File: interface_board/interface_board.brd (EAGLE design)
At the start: 72 x 56 mm, 103 parts, among them IC1 V7805-1000, IC6 LAN9512-JZX, K1 61400416021, Q6 CTS_32X25_SMD, U1 SFW15R-1STE1LF, U2 SFW15R-1STE1LF, U3 DMG1012T, U5 PAM2306DYPAA

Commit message: picam360
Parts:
- removed C11: UUD1A220MCL1GS(22u), resistor:153CLV-0405
- removed C15: UUD1E100MCL1GS(10u), resistor:153CLV-0405
- moved IC1 6.22 mm to (34.0, 28.8)
- moved R11 0.92 mm to (39.5, 28.4)
- moved R12 0.92 mm to (41.0, 28.4)
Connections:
- removed net 3V3A1: C32.2, C33.2, C34.2, C35.2, C36.2, C37.2, C38.2, FB2.1, IC6.10, IC6.49, IC6.5, IC6.51, IC6.54, IC6.57, IC6.64
- removed net N$47: IC6.1, JP5.D-
- removed net N$48: IC6.2, JP5.D+
- removed net USBD3_N: IC6.3, K1.2
- removed net USBD3_P: IC6.4, K1.3
- new net USB3_N: IC6.3, JP5.D-
- new net USB3_P: IC6.4, JP5.D+
- new net USBD2_N: IC6.1, K1.2
- new net USBD2_P: IC6.2, K1.3
- net +5V: no longer C11.+
- net 3V3A: now also C32.2, C33.2, C34.2, C35.2, C36.2, C37.2, C38.2, FB2.1, IC6.10, IC6.49, IC6.5, IC6.51, IC6.54, IC6.57, IC6.64
- net GND: no longer C11.-, C15.-
- net N$39: no longer C15.+
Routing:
- net 3V3A: track 11.6 -> 110.9 mm, vias 0 -> 8
- net 3V3A1: track 69.7 -> 0.00 mm, vias 7 -> 0
- net USB3_N: track 0.00 -> 30.0 mm, vias 0 -> 1
- net USB3_P: track 0.00 -> 29.3 mm, vias 0 -> 1
- net USBD2_N: track 0.00 -> 23.0 mm
- net USBD2_P: track 0.00 -> 22.3 mm
- net USBD3_N: track 22.0 -> 0.00 mm
- net USBD3_P: track 21.3 -> 0.00 mm
- net N$39: track 15.5 -> 20.9 mm
- net LAN_RUN: track 66.5 -> 67.6 mm
- net +5V: track 117.6 -> 116.8 mm, vias 3 -> 4
- net N$31: track 4.59 -> 5.37 mm
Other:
- board text added: "Picam360"
- board text removed: "OpenBLW"

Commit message: interface board
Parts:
- removed C16: 1u, resistor:C0402
- removed C17: 10n, resistor:C0402
- removed F1: MF-MSMF200-2, openblw:1812
- removed FB1, FB4: HR2220V801R-10, resistor:L5650M
- removed IC1: V7805-1000, openblw:DIP_3PIN
- removed JP2, JP3: M20-9980346, pinhead:2X03
- removed JP4: M20-9990246, openblw:1X02
- removed L3: SRP1245A-100M, openblw:SRP1250A
- removed R18: 1K, resistor:R0402
- removed U$1: 282836-2, openblw:282836-2
- removed U$2: M20-9980346, openblw:282836-2
- removed U$3: (no value), openblw:TENDA_P200
- JP1: device pinhead:2X04 -> pinhead:2X20
- moved R15 67.8 mm to (70.4, 23.8), flipped to the bottom
- moved R5 67.6 mm to (70.1, 51.4), turned to 270 degrees
- moved R6 67.2 mm to (69.8, 27.1), flipped to the bottom
- moved FB3 65.4 mm to (68.4, 35.1), flipped to the bottom
- moved FB2 65.4 mm to (68.4, 33.0), flipped to the bottom
- moved C28 65.1 mm to (68.4, 43.5), flipped to the bottom
- moved C27 65.1 mm to (68.3, 46.5), flipped to the bottom
- moved R32 65.1 mm to (68.4, 39.0), flipped to the bottom
- moved C29 65.1 mm to (68.4, 40.9), flipped to the bottom
- moved C43 65.0 mm to (68.3, 37.1), flipped to the bottom, turned to 180 degrees
- moved C4 64.4 mm to (68.1, 51.4), turned to 90 degrees
- moved R7 62.0 mm to (67.0, 30.4)
- moved R2 61.2 mm to (66.2, 51.3), turned to 90 degrees
- moved U3 60.8 mm to (66.4, 14.8), flipped to the bottom
- moved LED1 60.3 mm to (66.2, 20.4), flipped to the bottom
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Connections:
- removed net +12V: C16.1, F1.1, L3.2, U$2.CON1
- removed net AGND: FB4.1, JP2.5, JP2.6, U$1.CON1
- removed net AVCC: FB1.1, JP2.1, JP2.2, U$1.CON2
- removed net N$38: C17.1, R18.2
- removed net N$39: F1.2, IC1.IN
- removed net N$6: FB1.2, L3.1, R18.1
- net +3V3: no longer JP3.5, JP3.6, JP4.1
- net +5V: no longer IC1.OUT
- net GND: now also JP1.13, JP1.14; no longer C16.2, C17.2, FB4.2, IC1.GND, JP3.1, JP4.2, U$2.CON2
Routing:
- net +3V3: track 340.8 -> 0.00 mm, vias 21 -> 0
- net +5V: track 116.8 -> 0.00 mm, vias 4 -> 0
- net 3V3A: track 110.9 -> 0.00 mm, vias 8 -> 0
- net LAN_RUN: track 67.6 -> 0.00 mm, vias 3 -> 0
- net GND: track 65.5 -> 0.00 mm, vias 219 -> 0
- net TX_N: track 64.3 -> 0.00 mm
- net RX_P: track 60.4 -> 0.00 mm
- net TX_P: track 59.0 -> 0.00 mm
- net RX_N: track 57.3 -> 0.00 mm
- net CAM1_SCL: track 53.6 -> 0.00 mm, vias 2 -> 0
- net CAM1_SDA: track 53.1 -> 0.00 mm, vias 2 -> 0
- net UART0_TX: track 52.5 -> 0.00 mm, vias 1 -> 0
- net UART0_RX: track 51.5 -> 0.00 mm, vias 1 -> 0
- net +1V8: track 47.7 -> 0.00 mm, vias 3 -> 0
- net EXT1/UART1_RX: track 47.7 -> 0.00 mm, vias 1 -> 0
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- removed copper zone on layer 1, net +12V
- removed copper zone on layer 16, net +5V
- removed copper zone on layer 1, net AGND
- removed copper zone on layer 1, net AVCC
- removed copper zone on layer 1, net N$6
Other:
- outline, holes or cut-outs redrawn
- board text removed: "3V3"
- board text removed: "GND"

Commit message: refactoring
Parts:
- removed C12, C13, C14: 47u, resistor:C1206
- removed C4, C5: 100p, resistor:C0402
- removed C6, C7: 10u, resistor:C0805
- removed L1, L2: SRN4018-4R7M(4.7u), openblw:BOURNS-SRN4018
- removed PCB1: 1473005-4, openblw:RPI_COMPUTE
- removed R11, R12, R4, R5: 100K, resistor:R0402
- removed R13, R14, R16, R17: 1.8K, resistor:R0402
- removed R15, R6: 470R, resistor:R0402
- removed R7, R8, R9: 0R, resistor:R0805
- removed U3: DMG1012T, openblw:SOT523
- removed U5: PAM2306DYPAA, openblw:WDFN3X3-12L
- added C16: 1u, resistor:C0402
- added C17: 10n, resistor:C0402
- added FB1, FB4: HR2220V801R-10, resistor:L5650M
- added IC1: V7805-1000, openblw:DIP_3PIN
- added JP2, JP3: M20-9980346, pinhead+:2X03_SMT
- added JP4: (no value), pinhead:1X03
- added L3: SRP1245A-100M, openblw:SRP1250A
- added Q1: IRLML6346TRPBF, openblw:SOT23
- added R18: 1K, resistor:R0402
- added U$2, U$4, U$7, U$8: 282836-2, openblw:282836-2
- added U$3: (no value), openblw:TENDA_P200
- C10, C41, C42: device rcl:C0805 -> resistor:C0402
- C2: value 10u -> UWT1E221MNL1GS(220u); device resistor:C0805 -> resistor:153CLV-0810
- C21, C22, C23, C24, C26, C27, C28, C29, C30, C31, C32, C33, C34, C35, C36, C37, C38, C39, C40, C43, C44, C45, C8, C9: device rcl:C0603 -> resistor:C0402
- C3: value 10u -> 1uF; device resistor:C0805 -> SparkFun-Capacitors:0603-CAP
- JP1: value M20-9980446 -> M20-9990446; device pinhead:2X20 -> pinhead:2X05
- JP5: value USB-IDMICRO -> (none); device openblw:USB-MICRO -> pinhead:1X03
- LED1: value RED -> LTW-5630AZL50; device led:CHIP-LED0603 -> openblw:LITEON-5630
- LED2: value GREEN -> LTW-5630AZL50; device led:CHIP-LED0603 -> openblw:LITEON-5630
- R1: value 100K -> 4.99K
- R10, R19, R20, R25, R26, R27, R28, R29, R30, R31, R32, R33: device rcl:R0603 -> resistor:R0402
- R2: value 450K -> 100K
- R3: value 200K -> 1K
- U1: value SFW15R-1STE1LF -> AL5812MP-13; device openblw:RPI_CAMERA -> openblw:MSOP-8EP
- U2: value SFW15R-1STE1LF -> MPU-9250; device openblw:RPI_CAMERA -> invensense:LEAD-QFN24
- moved H4 78.6 mm to (3.50, 3.50), flipped to the top, turned to 180 degrees
- moved H3 73.3 mm to (61.5, 3.50), flipped to the top, turned to 180 degrees
- moved LOGO1 67.4 mm to (7.90, 71.9)
- moved LED1 62.6 mm to (4.00, 28.0), flipped to the top, turned to 180 degrees
- moved R2 57.7 mm to (16.9, 21.3), flipped to the top
- moved JP1 53.9 mm to (13.4, 52.5), flipped to the bottom, turned to 180 degrees
- moved H1 49.1 mm to (61.5, 52.5), flipped to the top, turned to 180 degrees
- moved H2 49.1 mm to (3.50, 52.5), flipped to the top, turned to 180 degrees
- moved C39 48.7 mm to (50.9, 4.57), flipped to the top, turned to 0 degrees
- moved R20 48.1 mm to (44.6, 4.57), flipped to the top, turned to 90 degrees
- moved C40 47.6 mm to (50.9, 5.84), flipped to the top, turned to 0 degrees
- moved C41 46.6 mm to (42.0, 7.75), flipped to the top, turned to 180 degrees
- moved C31 46.3 mm to (45.8, 4.57), flipped to the top
- moved C30 46.2 mm to (42.0, 5.21), flipped to the top, turned to 180 degrees
- moved R26 46.1 mm to (61.6, 45.1), turned to 90 degrees
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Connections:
- removed net +1V8: C5.1, C7.1, L2.P$1, R3.1, R9.2
- removed net BOTTOM_LIGHT_ENABLED: PCB1.59
- removed net CAM0_C_N: PCB1.144, U1.8
- removed net CAM0_C_P: PCB1.142, U1.9
- removed net CAM0_D0_N: PCB1.138, U1.2
- removed net CAM0_D0_P: PCB1.136, U1.3
- removed net CAM0_D1_N: PCB1.150, U1.5
- removed net CAM0_D1_P: PCB1.148, U1.6
- removed net CAM0_IO0: PCB1.36, U1.11
- removed net CAM0_IO1: PCB1.34, U1.12
- removed net CAM0_SCL: PCB1.30, R13.1, U1.13
- removed net CAM0_SDA: PCB1.28, R14.1, U1.14
- removed net CAM1_C_N: PCB1.149, U2.8
- removed net CAM1_C_P: PCB1.147, U2.9
- removed net CAM1_D0_N: PCB1.161, U2.2
- removed net CAM1_D0_P: PCB1.159, U2.3
- removed net CAM1_D1_N: PCB1.155, U2.5
- removed net CAM1_D1_P: PCB1.153, U2.6
- removed net CAM1_IO0: PCB1.11, U2.11
- removed net CAM1_IO1: PCB1.9, U2.12
- removed net CAM1_SCL: PCB1.5, R17.1, U2.13
- removed net CAM1_SDA: PCB1.3, R16.1, U2.14
- removed net CM_1V8: C12.1, PCB1.183, PCB1.184, PCB1.185, PCB1.186, R9.1
- removed net CM_3V3: C13.1, PCB1.189, PCB1.190, PCB1.191, PCB1.192, PCB1.193, PCB1.194, R8.1
- removed net CM_VBAT: C14.1, PCB1.197, PCB1.198, PCB1.199, PCB1.200, R7.1
- removed net EMMC_DISABLE_N: PCB1.2
- removed net EXT0/UART1_TX: JP1.6, PCB1.70
- removed net EXT1/UART1_RX: JP1.4, PCB1.72
- removed net GPIO47_1V8: PCB1.90, U3.1
- removed net N$10: C5.2, R3.2, R4.1, U5.10
- removed net N$11: PCB1.154
- removed net N$12: PCB1.156
- removed net N$13: PCB1.158
- removed net N$14: PCB1.160
- removed net N$15: PCB1.162
- removed net N$16: PCB1.10
- removed net N$17: PCB1.12
- removed net N$18: PCB1.14
- removed net N$19: PCB1.16
- removed net N$2: L1.P$2, U5.8
- removed net N$20: PCB1.18
- removed net N$21: PCB1.20
- removed net N$22: PCB1.22
- removed net N$23: PCB1.24
- removed net N$24: PCB1.124
- removed net N$25: PCB1.126
- removed net N$26: PCB1.128
- removed net N$27: PCB1.130
- removed net N$28: PCB1.132
- removed net N$29: PCB1.4
- removed net N$30: PCB1.6
- removed net N$31: PCB1.82, R12.1
- removed net N$32: LED2.A, R15.2
- removed net N$33: LED2.C, U3.3
- removed net N$34: PCB1.84, R11.1
- removed net N$35: PCB1.8
- removed net N$8: C4.2, R2.2, R5.1, U5.4
- removed net TOP_LIGHT_ENABLED: PCB1.57
- removed net UART0_RX: JP1.5, PCB1.53
- removed net UART0_TX: JP1.3, PCB1.51
- removed net USB3_N: IC6.3, JP5.D-
- removed net USB3_P: IC6.4, JP5.D+
- new net +12V: C1.2, C16.1, C2.+, IC1.IN, L3.2, LED1.A1, LED1.A2, LED1.A3, U$4.CON2, U1.1
- new net AGND: FB4.1, JP2.5, JP2.6, U$2.CON2
- new net AIN1: JP1.6
- new net AIN2: JP1.5
- new net AOUT1: U$8.CON1
- new net AOUT2: U$8.CON2
- new net AVCC: FB1.1, JP2.1, JP2.2, U$2.CON1
- new net BIN1: JP1.7
- new net BIN2: JP1.8
- new net BOUT1: U$7.CON2
- new net BOUT2: U$7.CON1
- new net LIGHT_PWM: JP1.1, R3.2
- new net N$38: C17.1, R18.2
- new net N$5: R1.2, U1.4
- new net N$6: Q1.3, R1.1
- new net PWMA: JP1.4
- new net PWMB: JP1.9
- new net TWI_SCL: U2.23
- new net TWI_SDA: U2.24
- new net VCC: U2.1, U2.13, U2.22, U2.8
- net +3V3: now also JP1.2, JP3.5, JP3.6; no longer C4.1, C6.1, L1.P$1, PCB1.39, PCB1.40, PCB1.41, PCB1.42, R13.2, R14.2, R15.1, R16.2, R17.2, R2.1, R6.1, R7.2, R8.2, U1.15, U2.15
- net +5V: now also IC1.OUT; no longer C2.1, C3.1, JP1.1, JP1.2, JP5.VBUS, R1.1, U5.1, U5.6, U5.7
- net GND: now also C1.1, C16.2, C17.2, C2.-, C3.1, FB4.2, IC1.GND, JP1.10, JP1.3, JP3.1, Q1.2, R2.1, U$4.CON1, U1.5, U1.HSINK, U2.11, U2.18, U2.20, U2.9; no longer C1.2, C12.2, C13.2, C14.2, C2.2, C3.2, C6.2, C7.2, JP1.13, JP1.14, JP1.7, JP1.8, JP5.GND, LED1.C, PCB1.1, PCB1.103, PCB1.104, PCB1.109, PCB1.110, PCB1.115, PCB1.121, PCB1.122, PCB1.127, PCB1.13, PCB1.133, PCB1.134, PCB1.139, PCB1.140, PCB1.145, PCB1.146, PCB1.151, PCB1.152, PCB1.157, PCB1.163, PCB1.164, PCB1.168, PCB1.169, PCB1.170, PCB1.181, PCB1.182, PCB1.187, PCB1.188, PCB1.19, PCB1.195, PCB1.196, PCB1.25, PCB1.26, PCB1.31, PCB1.32, PCB1.37, PCB1.38, PCB1.43, PCB1.44, PCB1.49, PCB1.50, PCB1.55, PCB1.56, PCB1.61, PCB1.62, PCB1.67, PCB1.68, PCB1.7, PCB1.73, PCB1.74, PCB1.79, PCB1.80, PCB1.85, PCB1.86, PCB1.91, PCB1.92, PCB1.97, PCB1.98, R11.2, R12.2, R4.2, R5.2, U1.1, U1.10, U1.4, U1.7, U2.1, U2.10, U2.4, U2.7, U3.2, U5.3, U5.9, U5.PAD
- net LAN_RUN: no longer PCB1.21
- net N$1: now also LED1.C1, LED1.C2, LED2.A1, LED2.A2, LED2.A3; no longer C1.1, R1.2, U5.12
- net N$3: now also FB1.2, L3.1, R18.1; no longer U5.5
- net N$4: now also C3.2, U2.10; no longer U5.11
- net N$7: now also Q1.1, R2.2, R3.1; no longer L2.P$2, U5.2
- net N$9: now also LED2.C1, LED2.C2, U1.8; no longer LED1.A, R6.2
- net USB_D_N: no longer PCB1.167
- net USB_D_P: no longer PCB1.165
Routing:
- net TX_N: track 0.00 -> 64.6 mm
- net TX_P: track 0.00 -> 64.0 mm
- net NLNKA_LED: track 0.00 -> 59.5 mm
- net NSPD_LED: track 0.00 -> 52.8 mm
- net RX_P: track 0.00 -> 40.0 mm
- net RX_N: track 0.00 -> 38.8 mm, vias 0 -> 1
- net +3V3: track 0.00 -> 29.7 mm, vias 0 -> 5
- net 3V3A: track 0.00 -> 24.5 mm, vias 0 -> 7
- net N$41: track 0.00 -> 11.7 mm
- net XO: track 0.00 -> 10.4 mm, vias 0 -> 1
- net XI: track 0.00 -> 9.83 mm, vias 0 -> 1
- net USBD2_N: track 0.00 -> 9.57 mm, vias 0 -> 1
- net USBD2_P: track 0.00 -> 9.55 mm, vias 0 -> 1
- net N$2: track 0.00 -> 7.62 mm
- net AVCC: track 0.00 -> 5.84 mm
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- added copper zone on layer 16, net +12V
- added copper zone on layer 16, net AGND
- added copper zone on layer 16, net AVCC
- added copper zone on layer 16, net N$3
- removed copper zone on layer 15, net GND
- removed copper zone on layer 2, net GND
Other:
- board size 72 x 56 mm -> 65 x 56 mm
- board text added: "Driver Board"
- board text added: "Rev.0.3"
- board text removed: "*"
- board text removed: "AVCC"
- board text removed: "CAM0"
- board text removed: "CAM1"
- board text removed: "Interface Board"
- board text removed: "Rev.0.5"

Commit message: refactoring
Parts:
- removed JP5: (no value), pinhead:1X03
- added JP6: USB-IDMICRO, openblw:USB-MICRO
- JP2, JP3: device pinhead+:2X03_SMT -> pinhead:2X03
- JP4: device pinhead:1X03 -> pinhead:2X03
- moved JP4 7.03 mm to (54.1, 52.3), flipped to the top, turned to 0 degrees
- moved C16 2.54 mm to (20.1, 13.7), turned to 180 degrees
- moved C2 1.62 mm to (23.1, 43.9), turned to 270 degrees
- moved C35 1.25 mm to (42.2, 12.3)
- moved C32 1.17 mm to (46.7, 12.3)
- moved C34 1.16 mm to (43.7, 12.3)
- moved C28 1.14 mm to (42.0, 10.4)
- moved C37 1.14 mm to (50.9, 9.78)
- moved C43 1.14 mm to (48.4, 19.9)
- moved C44 1.14 mm to (45.2, 16.8)
- moved C45 1.14 mm to (51.6, 16.8)
- moved FB3 1.14 mm to (47.8, 16.8)
- moved Q6 1.14 mm to (48.4, 16.8)
- moved R19 1.14 mm to (48.4, 19.3)
- moved R32 1.14 mm to (42.0, 9.14)
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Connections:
- net +5V: now also JP6.VBUS
- net GND: now also JP6.GND
- net USB_D_N: now also JP6.D-
- net USB_D_P: now also JP6.D+
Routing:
- net +3V3: track 29.7 -> 155.6 mm, vias 5 -> 7
- net +5V: track 2.18 -> 90.2 mm, vias 0 -> 2
- net +12V: track 1.71 -> 79.8 mm, vias 0 -> 3
- net N$1: track 1.30 -> 72.1 mm
- net N$9: track 0.00 -> 56.6 mm
- net AGND: track 5.84 -> 48.0 mm
- net AVCC: track 5.84 -> 41.0 mm
- net USB_D_N: track 0.00 -> 34.3 mm, vias 0 -> 1
- net LIGHT_PWM: track 0.00 -> 34.2 mm, vias 0 -> 1
- net USB_D_P: track 0.00 -> 33.6 mm, vias 0 -> 1
- net VDD18CORE: track 5.03 -> 22.8 mm
- net 3V3A: track 24.5 -> 38.7 mm
- net TX_P: track 64.0 -> 74.4 mm
- net RX_P: track 40.0 -> 49.5 mm
- net N$2: track 7.62 -> 0.00 mm
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
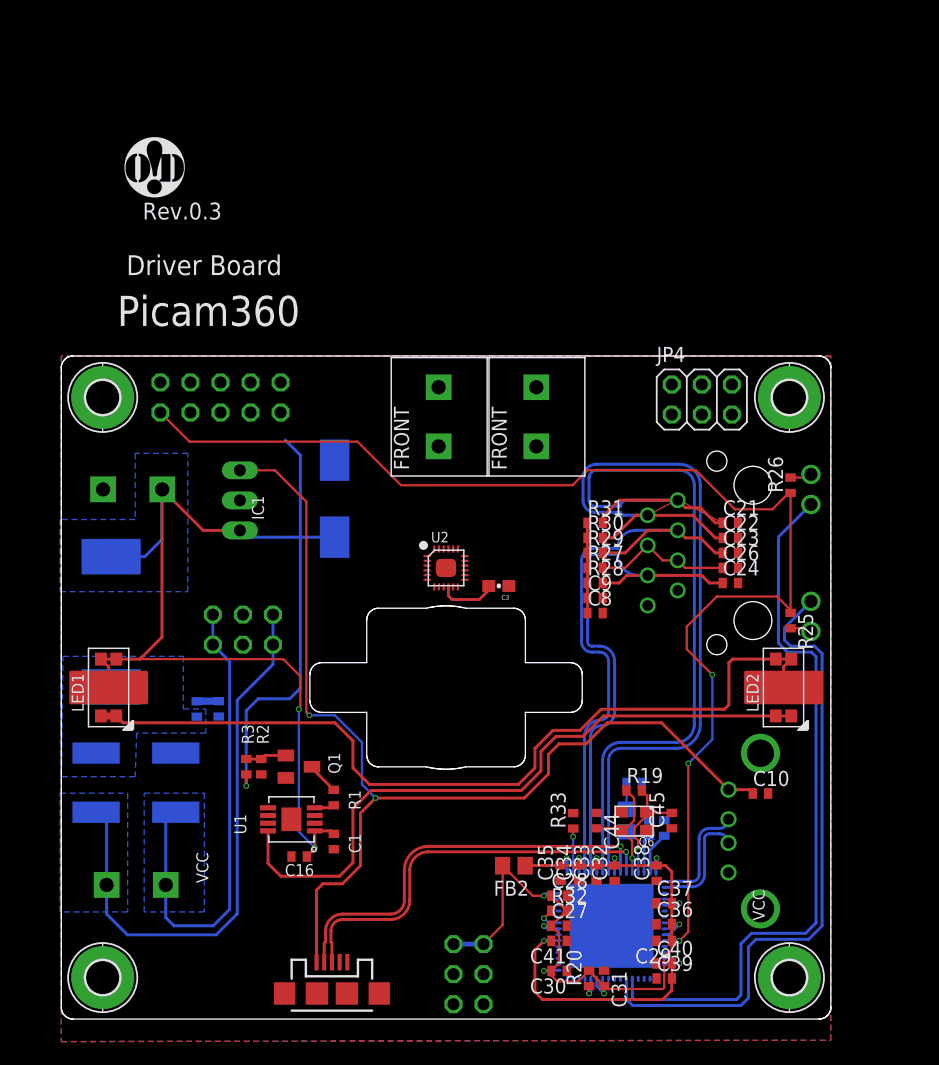
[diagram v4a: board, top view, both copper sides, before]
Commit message: interface_board provisional wiring
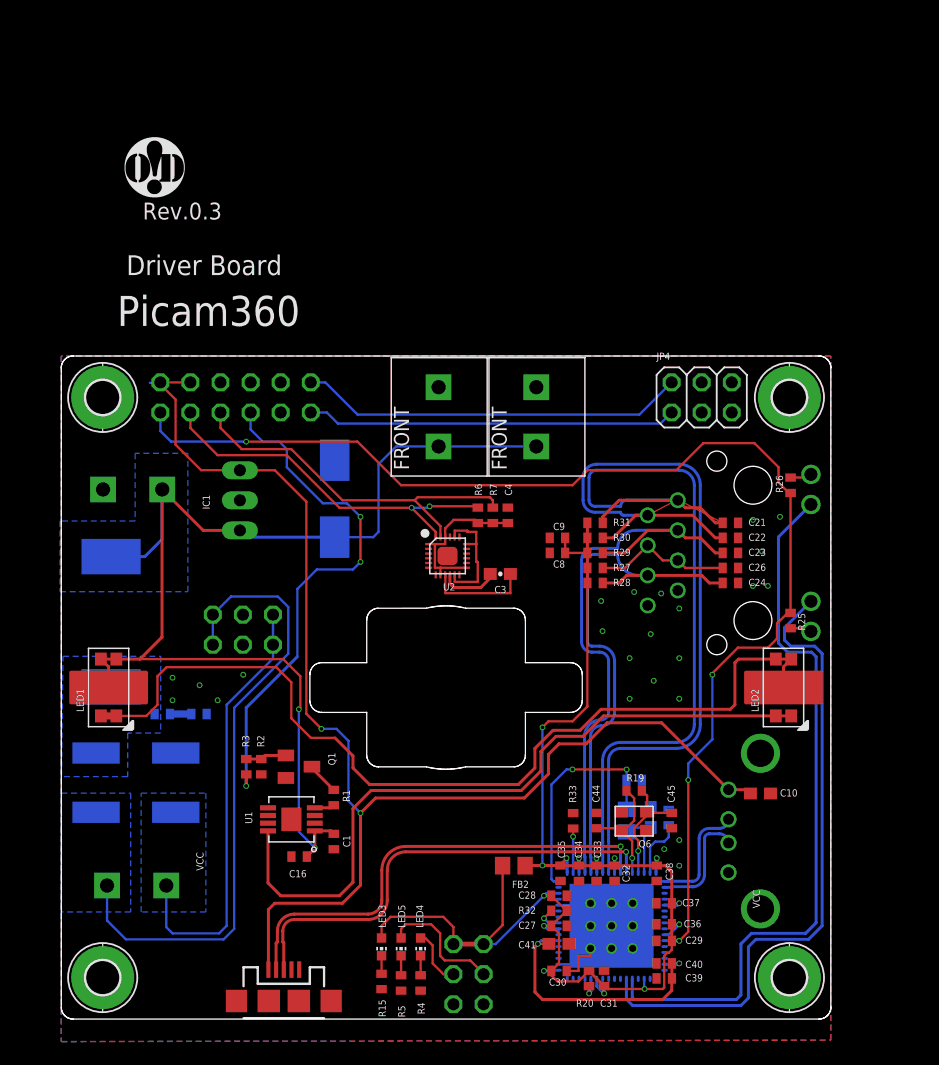
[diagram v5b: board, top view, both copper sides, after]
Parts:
- added C4: 100n, resistor:C0402
- added LED3, LED4, LED5: GREEN, led:CHIP-LED0603
- added R15, R4, R5: 470R, resistor:R0402
- added R6, R7: 10k, resistor:R0402
- C10, C41, C42: device resistor:C0402 -> resistor:C0603
- JP1: device pinhead:2X05 -> pinhead:2X06
- moved FB1 6.73 mm to (2.94, 20.0)
- moved FB4 6.73 mm to (9.67, 20.0)
- moved C8 5.99 mm to (41.9, 39.4), turned to 180 degrees
- moved C9 5.99 mm to (41.9, 40.6), turned to 180 degrees
- moved JP6 4.11 mm to (18.8, 1.52)
- moved R18 2.95 mm to (8.54, 25.8), turned to 180 degrees
- moved C17 1.72 mm to (11.6, 25.8), turned to 180 degrees
- moved JP1 1.27 mm to (14.7, 52.5)
- moved C3 1.02 mm to (37.1, 37.6)
- moved U2 1.02 mm to (32.6, 39.1)
- moved R10 0.97 mm to (51.3, 17.0)
- moved C42 0.90 mm to (49.8, 17.0)
- moved C43 0.25 mm to (48.4, 20.2)
- moved C41 0.25 mm to (42.0, 6.35)
- moved JP4 0.18 mm to (54.1, 52.5)
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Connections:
- removed net AIN1: JP1.6
- removed net AIN2: JP1.5
- removed net AOUT1: U$8.CON1
- removed net AOUT2: U$8.CON2
- removed net BIN1: JP1.7
- removed net BIN2: JP1.8
- removed net BOUT1: U$7.CON2
- removed net BOUT2: U$7.CON1
- new net N$11: JP3.4, LED5.A
- new net N$12: LED5.C, R5.1
- new net N$14: LED3.C, R15.1
- new net N$2: LED4.C, R4.1
- new net N$8: JP3.3, LED4.A
- net +12V: now also U$7.CON1, U$8.CON1
- net +3V3: now also LED3.A
- net +5V: now also JP1.1, JP1.3
- net GND: now also C4.1, JP1.5, JP3.2, R15.2, R4.2, R5.2, U$7.CON2, U$8.CON2; no longer JP1.3
- net LIGHT_PWM: now also JP1.8; no longer JP1.1
- net PWMA: now also JP1.12, JP4.1; no longer JP1.4
- net PWMB: now also JP1.11, JP4.2; no longer JP1.9
- net TWI_SCL: now also JP1.6, R7.1
- net TWI_SDA: now also JP1.4, R6.1
- net VCC: now also C4.2, R6.2, R7.2
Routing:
- net 3V3A: track 38.7 -> 72.2 mm, vias 7 -> 9
- net PWMB: track 0.00 -> 32.7 mm
- net TWI_SDA: track 0.00 -> 31.8 mm, vias 0 -> 2
- net TWI_SCL: track 0.00 -> 31.7 mm
- net PWMA: track 0.00 -> 31.3 mm
- net GND: track 0.00 -> 29.7 mm, vias 0 -> 33
- net +12V: track 79.8 -> 103.4 mm
- net +5V: track 90.2 -> 110.6 mm
- net VDD18PLL: track 2.23 -> 19.4 mm, vias 0 -> 2
- net VCC: track 0.00 -> 13.7 mm
- net AVCC: track 41.0 -> 53.7 mm
- net AGND: track 48.0 -> 37.0 mm
- net N$11: track 0.00 -> 10.8 mm
- net LIGHT_PWM: track 34.2 -> 44.2 mm, vias 1 -> 3
- net +3V3: track 155.6 -> 164.7 mm, vias 7 -> 9
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
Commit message: for 2017 version
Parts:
- removed K1: 61400416021, openblw:61400416021
- added K2: 61400826021, Wuerth_Elektronik_eiCan_Communication_Connectors_v2.2:61400826021
- added R8: 0, resistor:R0402
- added R9: 10k, resistor:R0402
- JP1: device pinhead:2X06 -> pinhead:2X08
- moved R10 6.83 mm to (46.4, 12.3), flipped to the top, turned to 90 degrees
- moved R33 3.05 mm to (40.2, 16.7)
- moved C42 2.92 mm to (46.9, 16.9)
- moved JP1 2.54 mm to (17.3, 52.5)
- moved C45 2.54 mm to (49.0, 16.8)
- moved Q6 2.54 mm to (45.8, 16.8)
- moved C31 2.41 mm to (43.4, 3.43)
- moved C33 2.41 mm to (42.8, 12.3)
- moved C34 2.41 mm to (41.3, 12.3)
- moved C35 2.41 mm to (39.8, 12.3)
- moved C38 2.41 mm to (47.9, 12.3)
- moved C44 2.41 mm to (42.8, 16.8)
- moved R19 2.41 mm to (46.0, 19.3)
- moved C27 2.41 mm to (39.6, 7.87)
- moved C28 2.41 mm to (39.6, 10.4)
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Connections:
- removed net VCC: C4.2, R6.2, R7.2, U2.1, U2.13, U2.22, U2.8
- new net N$10: JP1.14, R8.2
- new net USBD3_N: IC6.3, K2.B2
- new net USBD3_P: IC6.4, K2.B3
- net +3V3: now also C4.2, R6.2, R7.2, R9.2, U2.1, U2.13, U2.22, U2.8
- net +5V: now also K2.A1, K2.B1; no longer K1.1
- net GND: now also JP1.13, K2.A4, K2.B4; no longer K1.4
- net LAN_RUN: now also R8.1, R9.1
- net USBD2_N: now also K2.A2; no longer K1.2
- net USBD2_P: now also K2.A3; no longer K1.3
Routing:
- net N$10: track 0.00 -> 90.9 mm, vias 0 -> 1
- net +12V: track 103.4 -> 60.1 mm, vias 3 -> 2
- net AVCC: track 53.7 -> 28.5 mm
- net +3V3: track 164.7 -> 179.6 mm
- net VCC: track 13.7 -> 0.00 mm
- net N$1: track 78.0 -> 90.2 mm
- net USBD3_P: track 0.00 -> 10.7 mm
- net USBD3_N: track 0.00 -> 10.7 mm
- net AGND: track 37.0 -> 28.5 mm
- net LAN_RUN: track 0.00 -> 5.27 mm, vias 0 -> 1
- net +5V: track 110.6 -> 115.1 mm
- net USB_D_P: track 38.3 -> 35.9 mm
- net USB_D_N: track 39.0 -> 36.6 mm
- net PWMA: track 31.3 -> 33.7 mm
- net TX_N: track 72.1 -> 74.5 mm
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
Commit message: for 2017 first version
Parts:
- moved LOGO1 65.5 mm to (13.1, 6.61)
- moved C45 18.4 mm to (31.8, 10.4), turned to 0 degrees
- moved R19 18.2 mm to (28.8, 13.3), turned to 270 degrees
- moved Q6 14.5 mm to (31.8, 13.2), turned to 90 degrees
- moved C44 11.1 mm to (31.8, 16.0), turned to 0 degrees
- moved C4 8.59 mm to (29.2, 41.4), turned to 0 degrees
- moved R33 4.83 mm to (35.8, 14.7), turned to 180 degrees
- moved R26 4.20 mm to (61.8, 40.9), turned to 0 degrees
- moved R25 4.20 mm to (61.8, 37.8), turned to 0 degrees
- moved R10 4.12 mm to (49.8, 14.6), turned to 180 degrees
- moved C43 2.85 mm to (50.5, 18.9), flipped to the top, turned to 270 degrees
- moved C42 2.70 mm to (48.6, 18.9), flipped to the top
- moved R8 1.89 mm to (51.7, 3.17), turned to 270 degrees
- moved C3 1.27 mm to (37.1, 38.9)
- moved U2 1.27 mm to (32.6, 40.4)
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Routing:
- net +3V3: track 179.6 -> 213.3 mm
- net N$9: track 59.9 -> 85.1 mm
- net XI: track 9.80 -> 31.0 mm
- net XO: track 10.5 -> 26.5 mm
- net TX_N: track 74.5 -> 59.2 mm
- net TX_P: track 76.7 -> 63.2 mm
- net N$1: track 90.2 -> 77.8 mm
- net 3V3A: track 70.9 -> 82.7 mm
- net GND: track 30.8 -> 20.3 mm, vias 236 -> 226
- net USB_D_P: track 35.9 -> 46.3 mm
- net USB_D_N: track 36.6 -> 47.0 mm
- net +12V: track 60.1 -> 70.3 mm
- net VDD18PLL: track 19.9 -> 29.8 mm, vias 2 -> 1
- net N$40: track 1.83 -> 6.25 mm
- net N$37: track 1.83 -> 6.25 mm
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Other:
- board text added: "Interface Board"
- board text added: "Rev.0.4"
- board text removed: "Driver Board"
- board text removed: "Rev.0.3"

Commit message: pwr
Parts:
- removed U$3: (no value), openblw:TENDA_P200
- added U$1: (no value), openblw:TENDA_P200
- moved C4 7.42 mm to (36.4, 39.8), turned to 180 degrees
- moved C3 1.09 mm to (36.4, 38.0)
- moved R15 1.02 mm to (26.0, 3.05)
- moved LED4 1.02 mm to (29.3, 6.10)
- moved LED5 1.02 mm to (27.7, 6.10)
- moved R4 1.02 mm to (29.3, 3.05)
- moved R5 1.02 mm to (27.7, 3.05)
- moved LED3 1.02 mm to (26.0, 6.10)
- moved JP3 1.00 mm to (33.4, 3.94)
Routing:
- net GND: track 20.3 -> 17.9 mm
- net +3V3: track 213.3 -> 214.5 mm
